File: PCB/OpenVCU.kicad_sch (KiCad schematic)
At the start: 25 parts, among them U1 STM32H743VIT6, Y1 ABM8-8.000MHZ-18-D1X-T3, Y2 CM315D32768DZFT

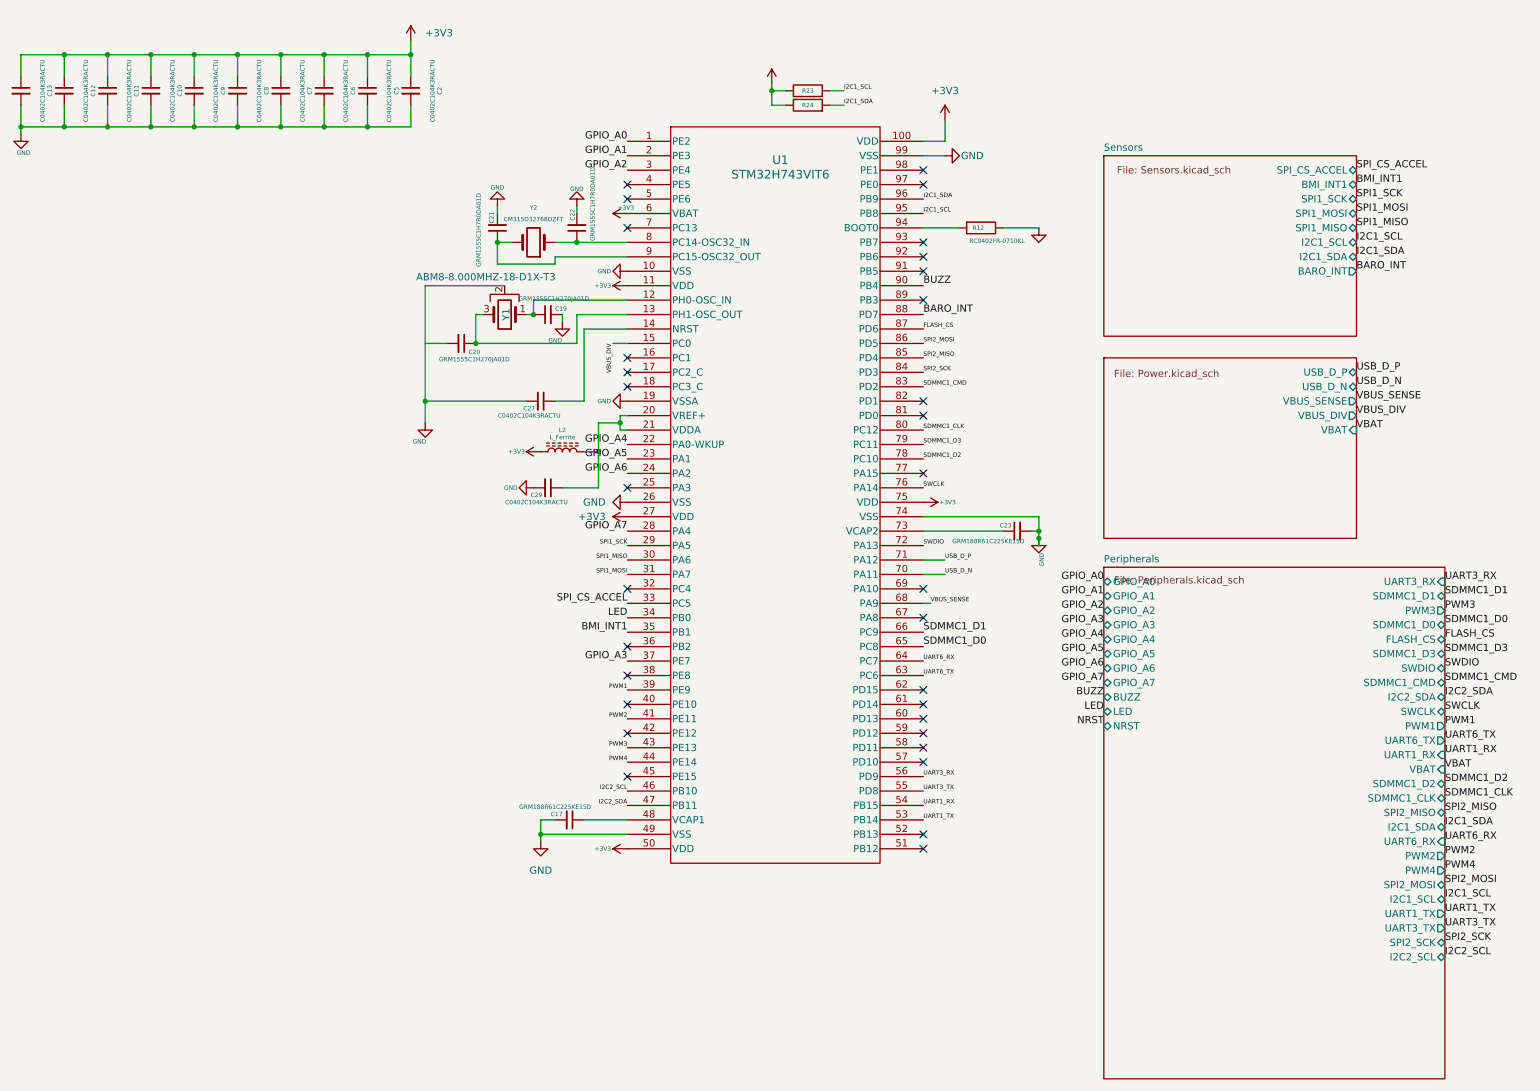
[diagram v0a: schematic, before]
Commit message: Power+root: drive every ERC error to zero
Power sheet
- add power:PWR_FLAG to the lib_symbols cache under its full lib_id so the
  flags actually resolve to a pin (a bare "PWR_FLAG" cache key resolves to
  zero pins and silently disables the flag)
- one PWR_FLAG per net: +5V, FB divider node, VBUS_SENSE
- name the TPS54360 divider node FB so R53/R54/R55 join U9.5's net
- wire U9.8 (SW) to the existing SW label (buck half-bridge)
- drop 12 orphan power symbols, the duplicate D_Schottky ref, R9/C28 and
  14 junk wires; re-point the USB-C CC pull-downs at Device:R
- rebuild the FB/COMP network to the standard TPS54360 divider
- label the USBLC6 pass-through pins USB_D_P/USB_D_N/VBUS_SENSE

Root sheet
- label NRST so the MCU reset net reaches the SWD header
- retarget C27 (NRST decoupling) from the oscillator rail to GND, with a real
  library symbol and footprint
- add PWR_FLAGs on GND, +3V3, VREF+, VCAP1 and VCAP2
- delete two dangling wire stubs

ERC: 240 errors -> 0.
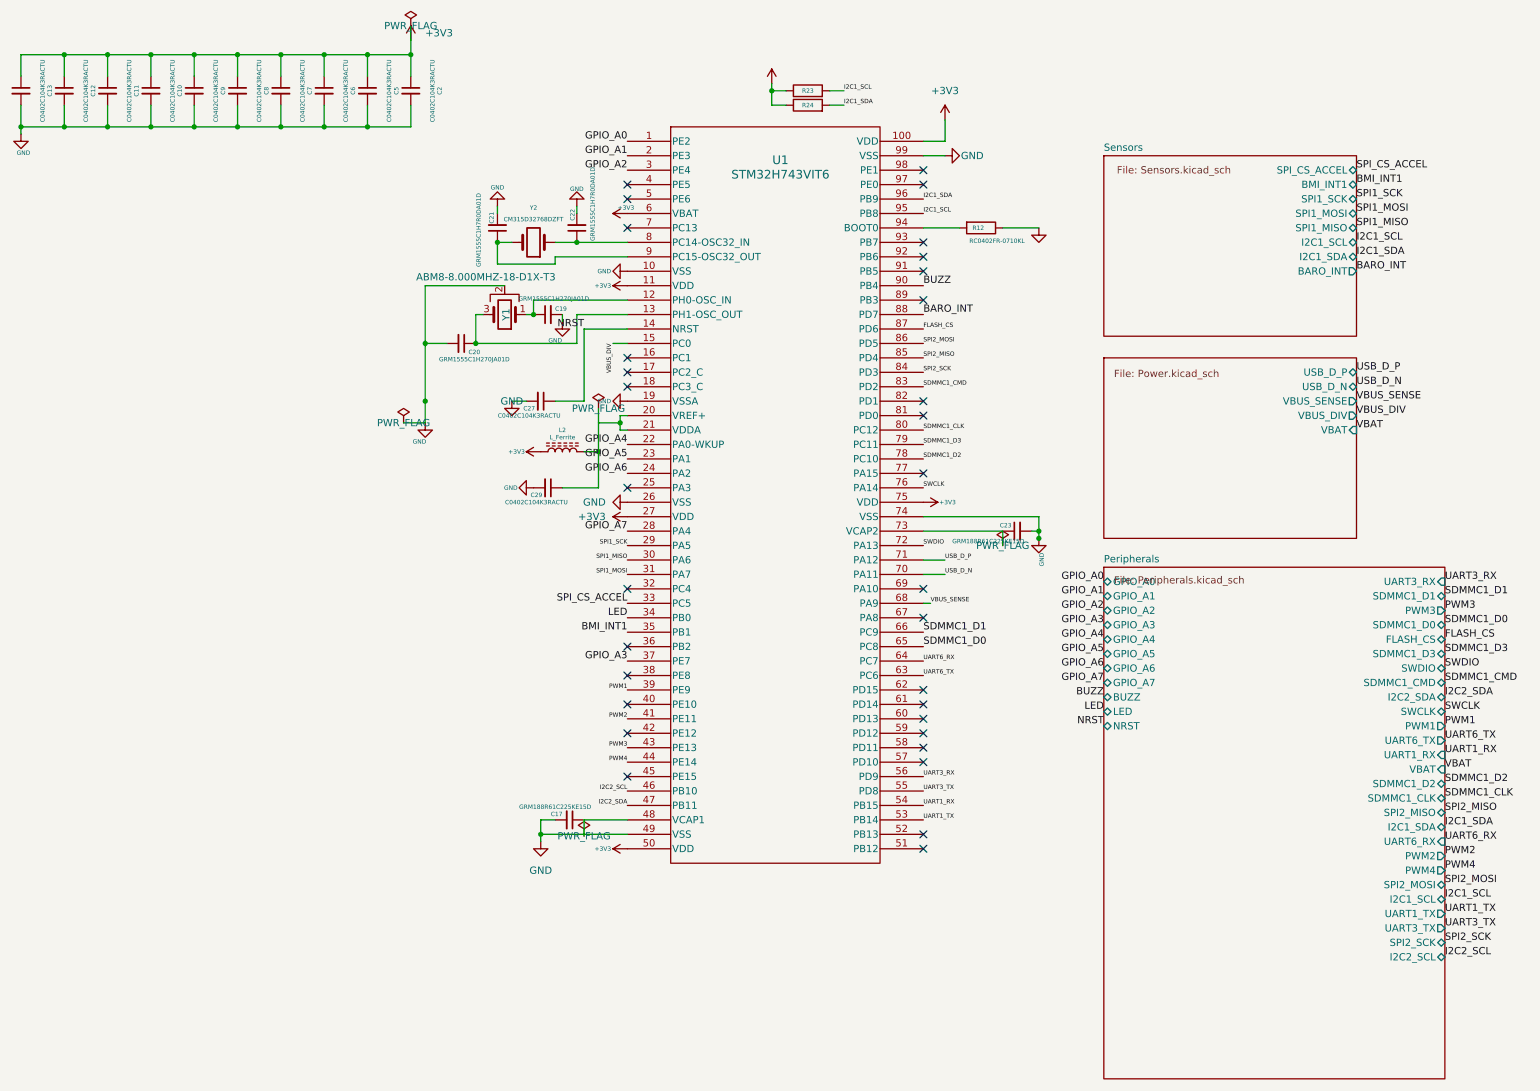
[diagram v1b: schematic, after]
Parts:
- C27: footprint C0402C104K3RACTU:CAPC1005X55N -> Capacitor_SMD:C_0402_1005Metric
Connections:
- net GND: now also C20.2
- net NRST: now also C27.1, U1.14 (NRST)

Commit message: Power: fix the shorted buck input rail (VBAT)
The buck input network was silently shorted to GND and had no VBAT net at all:

  * L1.1 (inductor, SW side) was wired to the +5V node instead of SW, shorting
    SW to +5V through the inductor
  * C51.2's GND stub passed straight through R50.1's pin, dragging the TPS54360
    feedback/EN divider top and VIN down to GND

Rebuild the VBAT tap and the +5V output node so that

  /Power/VBAT = C51.1, C52.1, C53.1, R50.1, U9.2 (VIN)
  /Power/SW   = C50.2, D1.1, L1.1, U9.8          (catch diode + inductor)
  +5V         = C55.1, C56.1, L1.2, R53.1, ...

Also drop the vestigial VBAT hierarchical pin (Power + Peripherals) and its two
root labels: nothing on the root or Peripherals sheets consumes battery voltage,
and the MCU VBAT pin is tied to +3V3 on the root, so it was dangling.
Add a PWR_FLAG on the VBAT rail.

New tools: /tmp/opencode/overlap.py and junctions.py detect collinear-overlap and
T-junction shorts, which ERC does not report.

ERC: 0 errors.
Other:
- sheet Peripherals ports: added none; removed VBAT
- sheet Power ports: added none; removed VBAT
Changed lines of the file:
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@@
 			(at 266.7 81.28 0)
 		)
-		(pin "VBAT" input
-			(at 266.7 83.82 0)
-		)
 		(instances
 			(project "OpenVCU"
@@
 			(at 282.25 140.97 0)
 		)
-		(pin "VBAT" input
-			(at 282.25 143.51 0)
-		)
 		(pin "SDMMC1_D2" bidirectional
 			(at 282.25 146.05 0)
@@
 	)
 	(embedded_fonts no)
-	(label "VBAT"
-		(at 266.7 83.82 0)
-		(effects
-			(font
-				(size 1.27 1.27)
-			)
-			(justify left bottom)
-		)
-	)
-	(label "VBAT"
-		(at 282.25 143.51 0)
-		(effects
-			(font
-				(size 1.27 1.27)
-			)
-			(justify left bottom)
-		)
-	)
 	(label "BARO_INT"
 		(at 266.7 55.88 0)

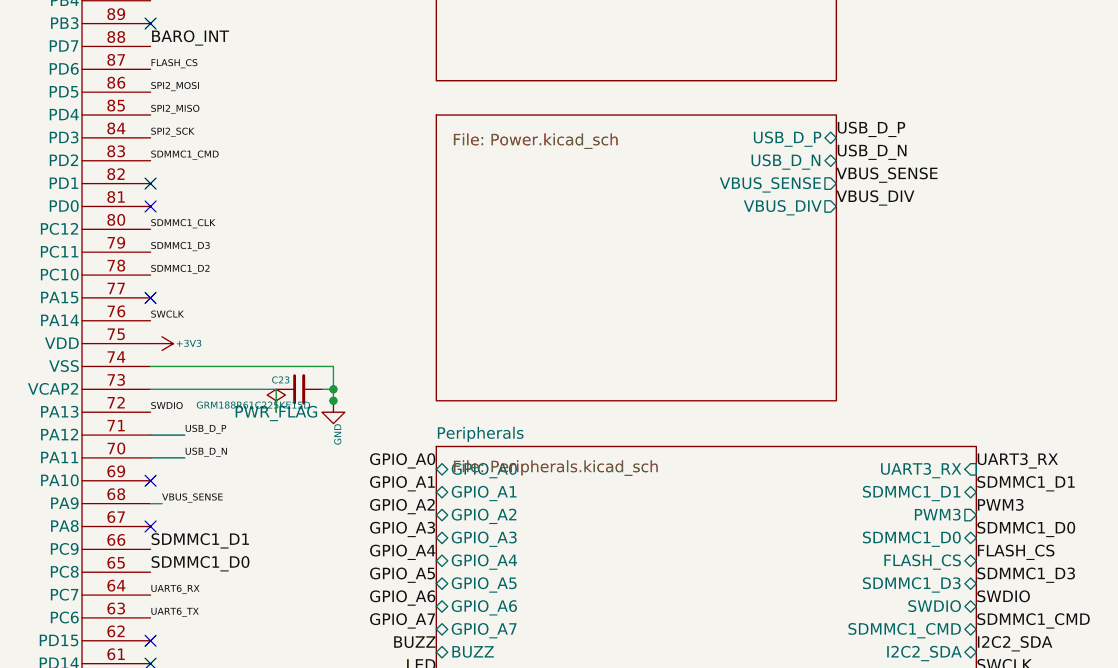
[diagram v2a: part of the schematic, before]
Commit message: Power/root: fix USB VBUS sensing and remove ambiguous net names
  * U1.68 (PA9) was wired straight to raw VBUS, so the MCU saw up to 20V
    instead of the divided voltage. It is now on VBUS_DIV, whose only other
    members are the R1/R5 divider tap and U1.15 (PC0)
  * the divider's top node is labelled VBUS, matching the USB-C VBUS pins and
    the USBLC6 VBUS pin, so there is no VBUS/VBUS_SENSE clash
  * drop the now-unused VBUS_SENSE hierarchical pin and its root label

ERC: 0 errors, 201 -> 190 warnings.
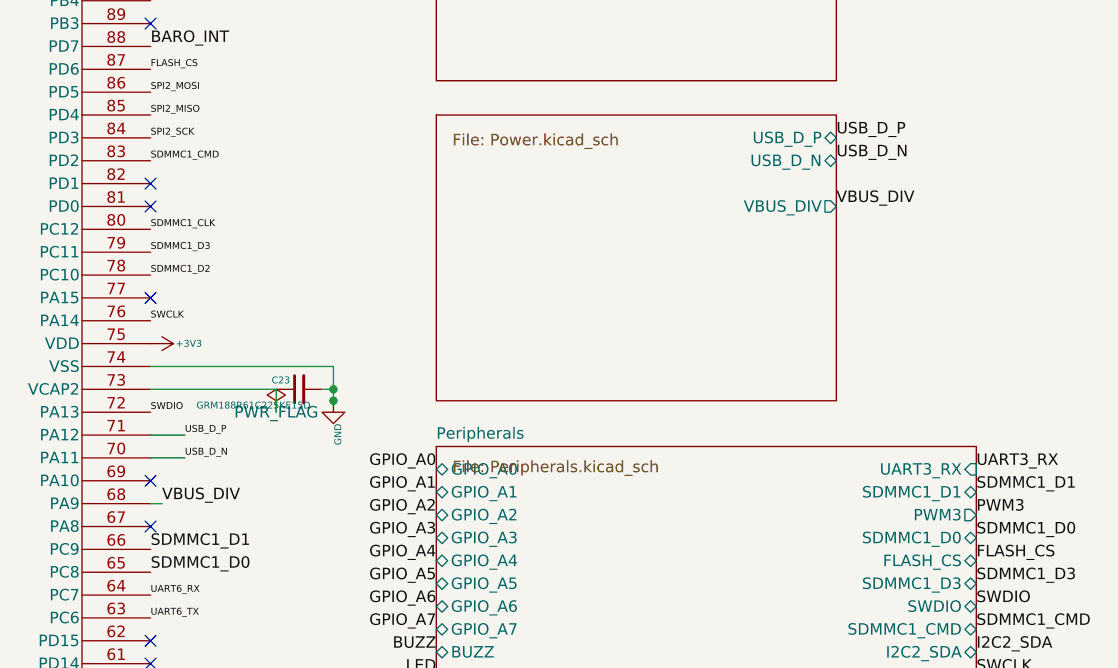
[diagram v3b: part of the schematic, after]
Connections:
- net VBUS_SENSE is gone; now on net VBUS_DIV: U1.68 (PA9)
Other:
- sheet Power ports: added none; removed VBUS_SENSE
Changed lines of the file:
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@@
 		)
 	)
-	(label "VBUS_SENSE"
-		(at 191.77 114.3 0)
-		(effects
-			(font
-				(size 0.762 0.762)
-			)
-			(justify left bottom)
-		)
-	)
 	(label "PWM4"
 		(at 138.43 142.24 180)
@@
 		)
 	)
-	(label "VBUS_SENSE"
-		(at 266.7 78.74 0)
-		(effects
-			(font
-				(size 1.27 1.27)
-			)
-			(justify left bottom)
-		)
-	)
 	(label "VBUS_DIV"
 		(at 266.7 81.28 0)
@@
 			(at 266.7 76.2 0)
 		)
-		(pin "VBUS_SENSE" output
-			(at 266.7 78.74 0)
-		)
 		(pin "VBUS_DIV" output
 			(at 266.7 81.28 0)
@@
 		)
 	)
+	(label "VBUS_DIV"
+		(at 191.77 114.3 0)
+		(effects
+			(font
+				(size 1.27 1.27)
+			)
+			(justify left bottom)
+		)
+	)
